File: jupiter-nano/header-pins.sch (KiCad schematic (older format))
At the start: 0 parts

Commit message: WIP, connectors almost done
- still to do:
  - JTAG signals on PIO pins
  - USB-UART bridge
  - extra PIO on the header pins
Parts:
- added J1, J2: Conn_01x20, symbol Connector_Generic:Conn_01x20
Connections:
- new net AD0: J1.10 (Pin_10)
- new net AD1: J1.7 (Pin_7)
- new net AD2: J1.6 (Pin_6)
- new net AD3: J1.9 (Pin_9)
- new net AD4: J1.5 (Pin_5)
- new net AD5: J1.8 (Pin_8)
- new net ADTRG-IRQ: J2.5 (Pin_5)
- new net ADVREF: J1.3 (Pin_3)
- new net FLEXCOM4_IO1: J2.4 (Pin_4)
- new net GND: J1.20 (Pin_20), J1.4 (Pin_4)
- new net I2C_TWCK0: J2.11 (Pin_11)
- new net I2C_TWD0: J2.12 (Pin_12)
- new net NC: J1.14 (Pin_14), J1.15 (Pin_15), J1.16 (Pin_16), J1.17 (Pin_17), J1.18 (Pin_18), J1.19 (Pin_19), J2.13 (Pin_13), J2.14 (Pin_14), J2.15 (Pin_15), J2.16 (Pin_16), J2.17 (Pin_17), J2.18 (Pin_18), J2.19 (Pin_19), J2.20 (Pin_20)
- new net POWER: J2.2 (Pin_2)
- new net PWMEXTRG-IRQ: J2.10 (Pin_10)
- new net PWMH1: J2.6 (Pin_6)
- new net PWMH2: J2.9 (Pin_9)
- new net PWMH3: J2.7 (Pin_7)
- new net PWML1: J2.8 (Pin_8)
- new net RESET: J1.1 (Pin_1)
- new net SPI0_MISO: J1.13 (Pin_13)
- new net SPI0_MOSI: J1.12 (Pin_12)
- new net SPI0_SCK: J1.11 (Pin_11)
- new net VBAT: J2.1 (Pin_1)
- new net VBUS: J2.3 (Pin_3)
- new net VDD_3V3: J1.2 (Pin_2)
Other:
- note added: "Header Pins"
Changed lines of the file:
@@
 Comment4 ""
 $EndDescr
+Text Notes 4600 2000 0    79   ~ 16
+Header Pins
+$Comp
+L Connector_Generic:Conn_01x20 J?
+U 1 1 6013FEF5
+P 4700 3400
+AR Path="/5F395F18/6013FEF5" Ref="J?"  Part="1"
+AR Path="/5F44311A/6013FEF5" Ref="J1"  Part="1"
+F 0 "J1" H 4650 4600 50  0000 L CNN
+F 1 "Conn_01x20" H 4450 4500 50  0000 L CNN
+F 2 "" H 4700 3400 50  0001 C CNN
+F 3 "~" H 4700 3400 50  0001 C CNN
+	1    4700 3400
+	1    0    0    -1
+$EndComp
+$Comp
+L Connector_Generic:Conn_01x20 J?
+U 1 1 6013FEFB
+P 6200 3400
+AR Path="/5F395F18/6013FEFB" Ref="J?"  Part="1"
+AR Path="/5F44311A/6013FEFB" Ref="J2"  Part="1"
+F 0 "J2" H 6150 4550 50  0000 C CNN
+F 1 "Conn_01x20" H 6150 4450 50  0000 C CNN
+F 2 "" H 6200 3400 50  0001 C CNN
+F 3 "~" H 6200 3400 50  0001 C CNN
+	1    6200 3400
+	-1   0    0    -1
+$EndComp
+Wire Wire Line
+	6400 2500 6800 2500
+Wire Wire Line
+	6400 2600 6800 2600
+Wire Wire Line
+	6400 2700 6800 2700
+Wire Wire Line
+	6400 2800 6800 2800
+Wire Wire Line
+	6400 2900 6800 2900
+Wire Wire Line
+	6400 3000 6800 3000
+Wire Wire Line
+	6400 3100 6800 3100
+Wire Wire Line
+	6400 3200 6800 3200
+Wire Wire Line
+	6400 3300 6800 3300
+Wire Wire Line
+	6400 3400 6800 3400
+Wire Wire Line
+	6400 3500 6800 3500
+Wire Wire Line
+	6400 3600 6800 3600
+Wire Wire Line
+	6400 3700 6800 3700
+Wire Wire Line
+	6400 3800 6800 3800
+Wire Wire Line
+	6400 3900 6800 3900
+Wire Wire Line
+	6400 4000 6800 4000
+Wire Wire Line
+	6400 4100 6800 4100
+Wire Wire Line
+	6400 4200 6800 4200
+Wire Wire Line
+	6400 4300 6800 4300
+Wire Wire Line
+	6400 4400 6800 4400
+Wire Wire Line
+	4100 2500 4500 2500
+Wire Wire Line
+	4500 2600 4100 2600
+Wire Wire Line
+	4500 2700 4100 2700
+Wire Wire Line
+	4500 2800 4100 2800
+Wire Wire Line
+	4500 2900 4100 2900
+Wire Wire Line
+	4500 3000 4100 3000
+Wire Wire Line
+	4500 3100 4100 3100
+Wire Wire Line
+	4500 3200 4100 3200
+Wire Wire Line
+	4500 3300 4100 3300
+Wire Wire Line
+	4500 3400 4100 3400
+Wire Wire Line
+	4500 3500 4100 3500
+Wire Wire Line
+	4500 3600 4100 3600
+Wire Wire Line
+	4500 3700 4100 3700
+Wire Wire Line
+	4500 3800 4100 3800
+Wire Wire Line
+	4500 3900 4100 3900
+Wire Wire Line
+	4500 4000 4100 4000
+Wire Wire Line
+	4500 4100 4100 4100
+Wire Wire Line
+	4500 4200 4100 4200
+Wire Wire Line
+	4500 4300 4100 4300
+Wire Wire Line
+	4500 4400 4100 4400
+Text GLabel 4100 2500 0    50   Input ~ 0
+RESET
+Text GLabel 4100 2600 0    50   Input ~ 0
+VDD_3V3
+Text GLabel 4100 2700 0    50   Input ~ 0
+ADVREF
+$Comp
+L power:GND #PWR?
+U 1 1 6015EE8C
+P 4100 2800
+F 0 "#PWR?" H 4100 2550 50  0001 C CNN
+F 1 "GND" V 4105 2672 50  0000 R CNN
+F 2 "" H 4100 2800 50  0001 C CNN
+F 3 "" H 4100 2800 50  0001 C CNN
+	1    4100 2800
+	0    1    1    0
+$EndComp
+Text GLabel 4100 2900 0    50   Input ~ 0
+AD4
+Text GLabel 4100 3000 0    50   Input ~ 0
+AD2
+Text GLabel 4100 3100 0    50   Input ~ 0
+AD1
+Text GLabel 4100 3200 0    50   Input ~ 0
+AD5
+Text GLabel 4100 3300 0    50   Input ~ 0
+AD3
+Text GLabel 4100 3400 0    50   Input ~ 0
+AD0
+$Comp
+L power:GND #PWR?
+U 1 1 6015F892
+P 4100 4400
+F 0 "#PWR?" H 4100 4150 50  0001 C CNN
+F 1 "GND" V 4105 4272 50  0000 R CNN
+F 2 "" H 4100 4400 50  0001 C CNN
+F 3 "" H 4100 4400 50  0001 C CNN
+	1    4100 4400
+	0    1    1    0
+$EndComp
+Text GLabel 4100 3500 0    50   Input ~ 0
+SPI0_SCK
+Text GLabel 4100 3600 0    50   Input ~ 0
+SPI0_MOSI
+Text GLabel 4100 3700 0    50   Input ~ 0
+SPI0_MISO
+Text GLabel 4100 3800 0    50   Input ~ 0
+NC
+Text GLabel 4100 3900 0    50   Input ~ 0
+NC
+Text GLabel 4100 4000 0    50   Input ~ 0
+NC
+Text GLabel 4100 4100 0    50   Input ~ 0
+NC
+Text GLabel 4100 4200 0    50   Input ~ 0
+NC
+Text GLabel 4100 4300 0    50   Input ~ 0
+NC
+Text GLabel 6800 2500 2    50   Input ~ 0
+VBAT
+Text GLabel 6800 2600 2    50   Input ~ 0
+POWER
+Text GLabel 6800 2700 2    50   Input ~ 0
+VBUS
+Text GLabel 6800 2800 2    50   Input ~ 0
+FLEXCOM4_IO1
+Text GLabel 6800 2900 2    50   Input ~ 0
+ADTRG-IRQ
+Text GLabel 6800 3000 2    50   Input ~ 0
+PWMH1
+Text GLabel 6800 3100 2    50   Input ~ 0
+PWMH3
+Text GLabel 6800 3200 2    50   Input ~ 0
+PWML1
+Text GLabel 6800 3300 2    50   Input ~ 0
+PWMH2
+Text GLabel 6800 3400 2    50   Input ~ 0
+PWMEXTRG-IRQ
+Text GLabel 6800 3500 2    50   Input ~ 0
+I2C_TWCK0
+Text GLabel 6800 3600 2    50   Input ~ 0
+I2C_TWD0
+Text GLabel 6800 3700 2    50   Input ~ 0
+NC
+Text GLabel 6800 3800 2    50   Input ~ 0
+NC
+Text GLabel 6800 3900 2    50   Input ~ 0
+NC
+Text GLabel 6800 4000 2    50   Input ~ 0
+NC
+Text GLabel 6800 4200 2    50   Input ~ 0
+NC
+Text GLabel 6800 4100 2    50   Input ~ 0
+NC
+Text GLabel 6800 4300 2    50   Input ~ 0
+NC
+Text GLabel 6800 4400 2    50   Input ~ 0
+NC
 $EndSCHEMATC

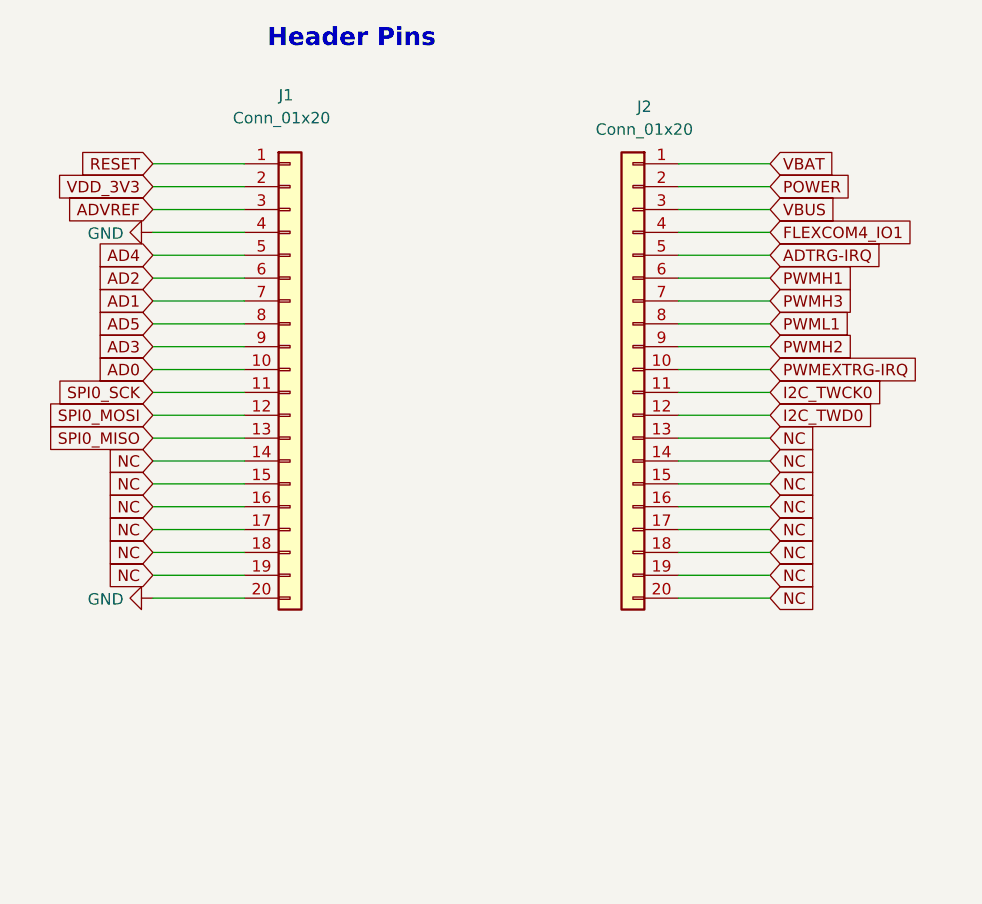
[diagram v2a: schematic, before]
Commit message: reset logic R names, values; longer connnectors
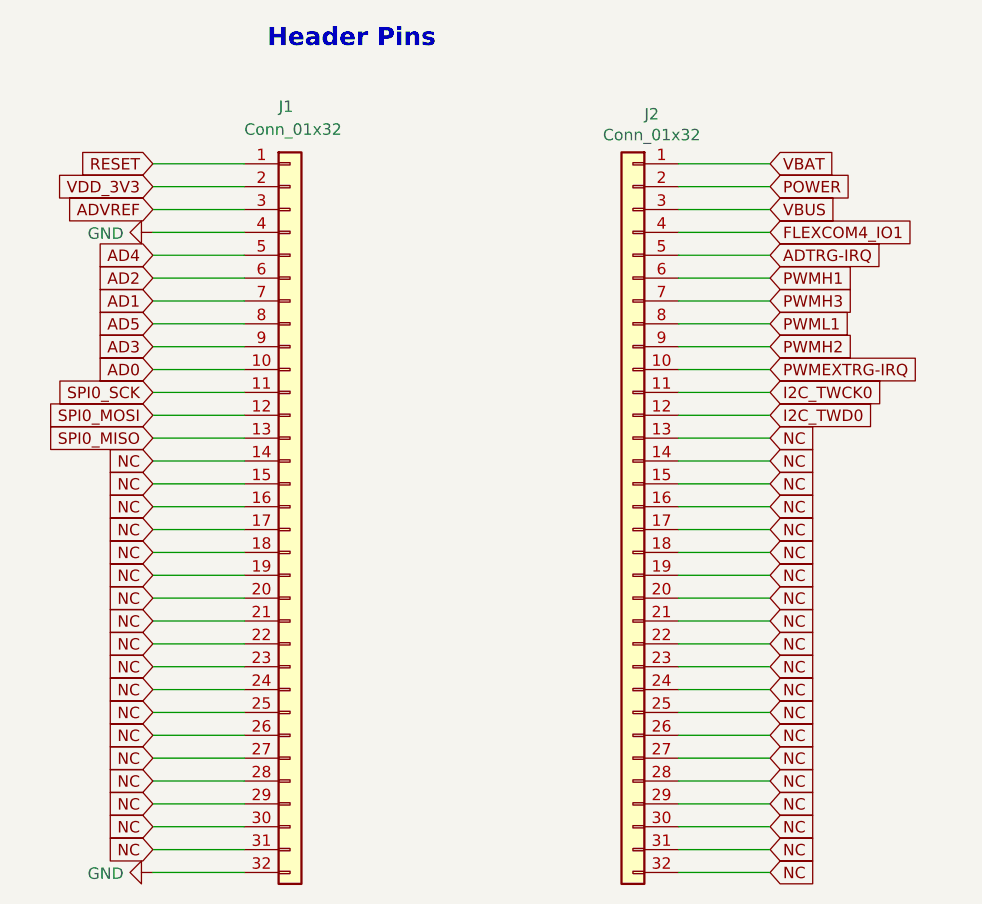
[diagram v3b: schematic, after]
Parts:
- removed J1, J2: Conn_01x20, symbol Connector_Generic:Conn_01x20
- added J1, J2: Conn_01x32, symbol Connector_Generic:Conn_01x32
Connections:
- net AD0: now also J1.10 (Pin_10)
- net AD1: now also J1.7 (Pin_7)
- net AD2: now also J1.6 (Pin_6)
- net AD3: now also J1.9 (Pin_9)
- net AD4: now also J1.5 (Pin_5)
- net AD5: now also J1.8 (Pin_8)
- net ADTRG-IRQ: now also J2.5 (Pin_5)
- net ADVREF: now also J1.3 (Pin_3)
- net FLEXCOM4_IO1: now also J2.4 (Pin_4)
- net GND: now also J1.32 (Pin_32), J1.4 (Pin_4)
- net I2C_TWCK0: now also J2.11 (Pin_11)
- net I2C_TWD0: now also J2.12 (Pin_12)
- net NC: now also J1.14 (Pin_14), J1.15 (Pin_15), J1.16 (Pin_16), J1.17 (Pin_17), J1.18 (Pin_18), J1.19 (Pin_19), J1.20 (Pin_20), J1.21 (Pin_21), J1.22 (Pin_22), J1.23 (Pin_23), J1.24 (Pin_24), J1.25 (Pin_25), J1.26 (Pin_26), J1.27 (Pin_27), J1.28 (Pin_28), J1.29 (Pin_29), J1.30 (Pin_30), J1.31 (Pin_31), J2.13 (Pin_13), J2.14 (Pin_14), J2.15 (Pin_15), J2.16 (Pin_16), J2.17 (Pin_17), J2.18 (Pin_18), J2.19 (Pin_19), J2.20 (Pin_20), J2.21 (Pin_21), J2.22 (Pin_22), J2.23 (Pin_23), J2.24 (Pin_24), J2.25 (Pin_25), J2.26 (Pin_26), J2.27 (Pin_27), J2.28 (Pin_28), J2.29 (Pin_29), J2.30 (Pin_30), J2.31 (Pin_31), J2.32 (Pin_32)
- net POWER: now also J2.2 (Pin_2)
- net PWMEXTRG-IRQ: now also J2.10 (Pin_10)
- net PWMH1: now also J2.6 (Pin_6)
- net PWMH2: now also J2.9 (Pin_9)
- net PWMH3: now also J2.7 (Pin_7)
- net PWML1: now also J2.8 (Pin_8)
- net RESET: now also J1.1 (Pin_1)
- net SPI0_MISO: now also J1.13 (Pin_13)
- net SPI0_MOSI: now also J1.12 (Pin_12)
- net SPI0_SCK: now also J1.11 (Pin_11)
- net VBAT: now also J2.1 (Pin_1)
- net VBUS: now also J2.3 (Pin_3)
- net VDD_3V3: now also J1.2 (Pin_2)
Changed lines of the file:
@@
 Text Notes 4600 2000 0    79   ~ 16
 Header Pins
-$Comp
-L Connector_Generic:Conn_01x20 J?
-U 1 1 6013FEF5
-P 4700 3400
-AR Path="/5F395F18/6013FEF5" Ref="J?"  Part="1"
-AR Path="/5F44311A/6013FEF5" Ref="J1"  Part="1"
-F 0 "J1" H 4650 4600 50  0000 L CNN
-F 1 "Conn_01x20" H 4450 4500 50  0000 L CNN
-F 2 "" H 4700 3400 50  0001 C CNN
-F 3 "~" H 4700 3400 50  0001 C CNN
-	1    4700 3400
-	1    0    0    -1
-$EndComp
-$Comp
-L Connector_Generic:Conn_01x20 J?
-U 1 1 6013FEFB
-P 6200 3400
-AR Path="/5F395F18/6013FEFB" Ref="J?"  Part="1"
-AR Path="/5F44311A/6013FEFB" Ref="J2"  Part="1"
-F 0 "J2" H 6150 4550 50  0000 C CNN
-F 1 "Conn_01x20" H 6150 4450 50  0000 C CNN
-F 2 "" H 6200 3400 50  0001 C CNN
-F 3 "~" H 6200 3400 50  0001 C CNN
-	1    6200 3400
-	-1   0    0    -1
-$EndComp
 Wire Wire Line
 	6400 2500 6800 2500
@@
 Wire Wire Line
 	4500 4300 4100 4300
-Wire Wire Line
-	4500 4400 4100 4400
 Text GLabel 4100 2500 0    50   Input ~ 0
 RESET
@@
 L power:GND #PWR?
 U 1 1 6015F892
-P 4100 4400
-F 0 "#PWR?" H 4100 4150 50  0001 C CNN
-F 1 "GND" V 4105 4272 50  0000 R CNN
-F 2 "" H 4100 4400 50  0001 C CNN
-F 3 "" H 4100 4400 50  0001 C CNN
-	1    4100 4400
+P 4100 5600
+F 0 "#PWR?" H 4100 5350 50  0001 C CNN
+F 1 "GND" V 4105 5472 50  0000 R CNN
+F 2 "" H 4100 5600 50  0001 C CNN
+F 3 "" H 4100 5600 50  0001 C CNN
+	1    4100 5600
 	0    1    1    0
 $EndComp
@@
 Text GLabel 6800 4400 2    50   Input ~ 0
 NC
+Wire Wire Line
+	4500 5600 4100 5600
+Wire Wire Line
+	4500 4400 4100 4400
+Wire Wire Line
+	4500 4500 4100 4500
+Wire Wire Line
+	4500 4600 4100 4600
+Wire Wire Line
+	4500 4700 4100 4700
+Wire Wire Line
+	4500 4800 4100 4800
+Wire Wire Line
+	4500 4900 4100 4900
+Wire Wire Line
+	4500 5000 4100 5000
+Wire Wire Line
+	4500 5100 4100 5100
+Wire Wire Line
+	4500 5200 4100 5200
+Wire Wire Line
+	4500 5300 4100 5300
+Wire Wire Line
+	4500 5400 4100 5400
+Wire Wire Line
+	4500 5500 4100 5500
+Text GLabel 4100 4400 0    50   Input ~ 0
+NC
+Text GLabel 4100 4500 0    50   Input ~ 0
+NC
+Text GLabel 4100 4600 0    50   Input ~ 0
+NC
+Text GLabel 4100 4700 0    50   Input ~ 0
+NC
+Text GLabel 4100 4800 0    50   Input ~ 0
+NC
+Text GLabel 4100 4900 0    50   Input ~ 0
+NC
+Text GLabel 4100 5000 0    50   Input ~ 0
+NC
+Text GLabel 4100 5100 0    50   Input ~ 0
+NC
+Text GLabel 4100 5200 0    50   Input ~ 0
+NC
+Text GLabel 4100 5300 0    50   Input ~ 0
+NC
+Text GLabel 4100 5400 0    50   Input ~ 0
+NC
+Text GLabel 4100 5500 0    50   Input ~ 0
+NC
+Wire Wire Line
+	6400 4500 6800 4500
+Wire Wire Line
+	6400 4600 6800 4600
+Wire Wire Line
+	6400 4700 6800 4700
+Wire Wire Line
+	6400 4800 6800 4800
+Wire Wire Line
+	6400 4900 6800 4900
+Wire Wire Line
+	6400 5000 6800 5000
+Wire Wire Line
+	6400 5100 6800 5100
+Wire Wire Line
+	6400 5200 6800 5200
+Text GLabel 6800 4500 2    50   Input ~ 0
+NC
+Text GLabel 6800 4600 2    50   Input ~ 0
+NC
+Text GLabel 6800 4700 2    50   Input ~ 0
+NC
+Text GLabel 6800 4800 2    50   Input ~ 0
+NC
+Text GLabel 6800 5000 2    50   Input ~ 0
+NC
+Text GLabel 6800 4900 2    50   Input ~ 0
+NC
+Text GLabel 6800 5100 2    50   Input ~ 0
+NC
+Text GLabel 6800 5200 2    50   Input ~ 0
+NC
+Wire Wire Line
+	6400 5300 6800 5300
+Wire Wire Line
+	6400 5400 6800 5400
+Wire Wire Line
+	6400 5500 6800 5500
+Wire Wire Line
+	6400 5600 6800 5600
+Text GLabel 6800 5400 2    50   Input ~ 0
+NC
+Text GLabel 6800 5300 2    50   Input ~ 0
+NC
+Text GLabel 6800 5500 2    50   Input ~ 0
+NC
+Text GLabel 6800 5600 2    50   Input ~ 0
+NC
+$Comp
+L Connector_Generic:Conn_01x32 J1
+U 1 1 6025EA16
+P 4700 4000
+F 0 "J1" H 4650 5750 50  0000 L CNN
+F 1 "Conn_01x32" H 4500 5650 50  0000 L CNN
+F 2 "" H 4700 4000 50  0001 C CNN
+F 3 "~" H 4700 4000 50  0001 C CNN
+	1    4700 4000
+	1    0    0    -1
+$EndComp
+$Comp
+L Connector_Generic:Conn_01x32 J2
+U 1 1 60262515
+P 6200 4000
+F 0 "J2" H 6118 5717 50  0000 C CNN
+F 1 "Conn_01x32" H 6118 5626 50  0000 C CNN
+F 2 "" H 6200 4000 50  0001 C CNN
+F 3 "~" H 6200 4000 50  0001 C CNN
+	1    6200 4000
+	-1   0    0    -1
+$EndComp
 $EndSCHEMATC

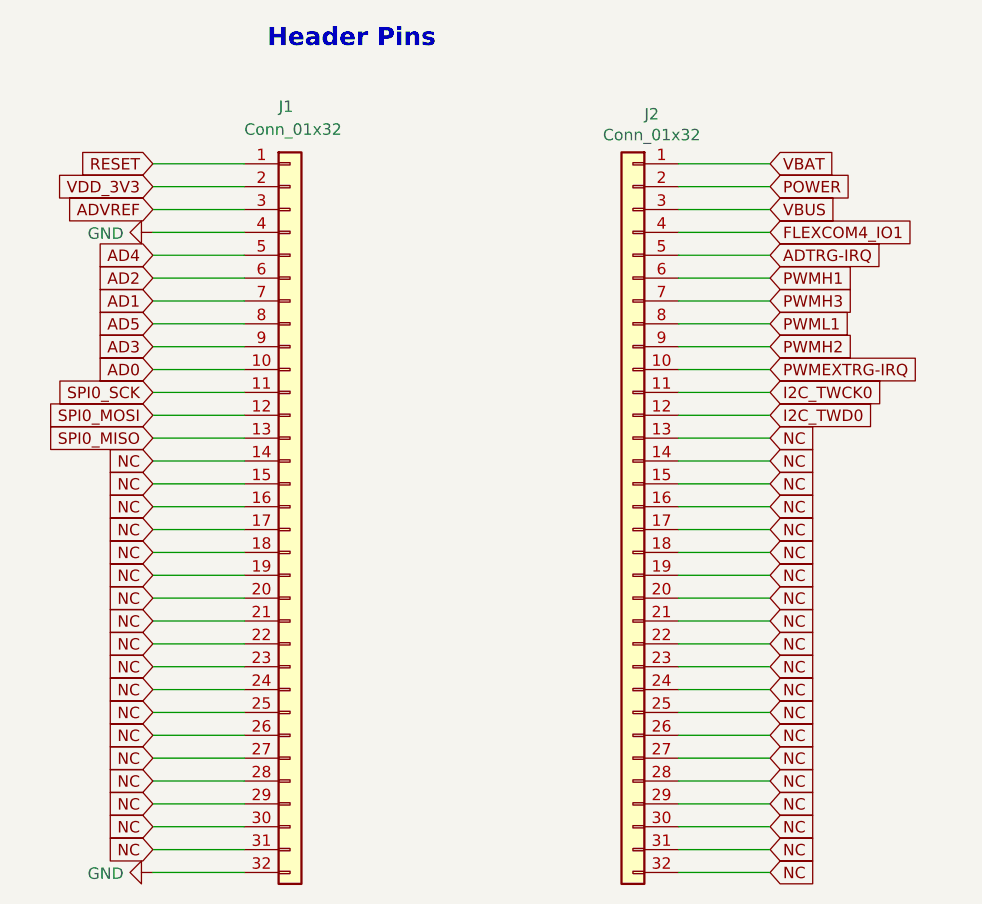
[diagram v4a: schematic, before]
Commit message: numerous ERC fixes
- still more to go
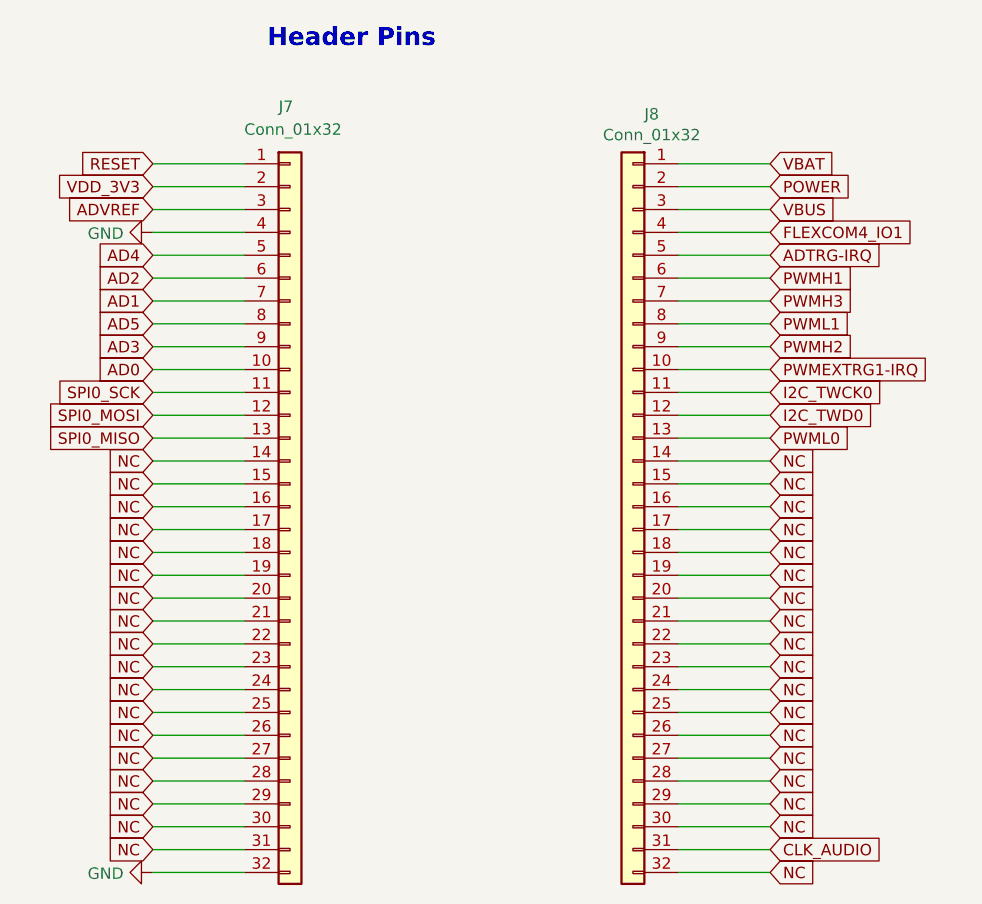
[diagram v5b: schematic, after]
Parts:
- renumbered J1 to J7, J2 to J8
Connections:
- net NC: no longer J8.13 (Pin_13), J8.31 (Pin_31)
- net PWMEXTRG-IRQ renamed PWMEXTRG1-IRQ
- new net CLK_AUDIO: J8.31 (Pin_31)
- new net PWML0: J8.13 (Pin_13)
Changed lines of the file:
@@
 	6400 3100 6800 3100
 Wire Wire Line
-	6400 3200 6800 3200
-Wire Wire Line
 	6400 3300 6800 3300
 Wire Wire Line
-	6400 3400 6800 3400
-Wire Wire Line
 	6400 3500 6800 3500
 Wire Wire Line
@@
 Wire Wire Line
 	4500 3400 4100 3400
-Wire Wire Line
-	4500 3500 4100 3500
-Wire Wire Line
-	4500 3600 4100 3600
-Wire Wire Line
-	4500 3700 4100 3700
 Wire Wire Line
 	4500 3800 4100 3800
@@
 ADVREF
 $Comp
-L power:GND #PWR0121
+L power:GND #PWR022
 U 1 1 6015EE8C
 P 4100 2800
-F 0 "#PWR0121" H 4100 2550 50  0001 C CNN
+F 0 "#PWR022" H 4100 2550 50  0001 C CNN
 F 1 "GND" V 4105 2672 50  0000 R CNN
 F 2 "" H 4100 2800 50  0001 C CNN
@@
 AD0
 $Comp
-L power:GND #PWR0122
+L power:GND #PWR023
 U 1 1 6015F892
 P 4100 5600
-F 0 "#PWR0122" H 4100 5350 50  0001 C CNN
+F 0 "#PWR023" H 4100 5350 50  0001 C CNN
 F 1 "GND" V 4105 5472 50  0000 R CNN
 F 2 "" H 4100 5600 50  0001 C CNN
@@
 PWMH2
 Text GLabel 6800 3400 2    50   Input ~ 0
-PWMEXTRG-IRQ
+PWMEXTRG1-IRQ
 Text GLabel 6800 3500 2    50   Input ~ 0
 I2C_TWCK0
@@
 I2C_TWD0
 Text GLabel 6800 3700 2    50   Input ~ 0
-NC
+PWML0
 Text GLabel 6800 3800 2    50   Input ~ 0
 NC
@@
 NC
 Text GLabel 6800 5500 2    50   Input ~ 0
-NC
+CLK_AUDIO
 Text GLabel 6800 5600 2    50   Input ~ 0
 NC
 $Comp
-L Connector_Generic:Conn_01x32 J1
+L Connector_Generic:Conn_01x32 J7
 U 1 1 6025EA16
 P 4700 4000
-F 0 "J1" H 4650 5750 50  0000 L CNN
+F 0 "J7" H 4650 5750 50  0000 L CNN
 F 1 "Conn_01x32" H 4500 5650 50  0000 L CNN
 F 2 "" H 4700 4000 50  0001 C CNN
@@
 $EndComp
 $Comp
-L Connector_Generic:Conn_01x32 J2
+L Connector_Generic:Conn_01x32 J8
 U 1 1 60262515
 P 6200 4000
-F 0 "J2" H 6118 5717 50  0000 C CNN
+F 0 "J8" H 6118 5717 50  0000 C CNN
 F 1 "Conn_01x32" H 6118 5626 50  0000 C CNN
 F 2 "" H 6200 4000 50  0001 C CNN
@@
 	-1   0    0    -1
 $EndComp
+Wire Wire Line
+	6400 3200 6800 3200
+Wire Wire Line
+	6400 3400 6800 3400
+Wire Wire Line
+	4100 3500 4500 3500
+Wire Wire Line
+	4100 3600 4500 3600
+Wire Wire Line
+	4100 3700 4500 3700
 $EndSCHEMATC
